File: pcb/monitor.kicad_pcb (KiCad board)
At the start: 2 copper layers, 53 parts, among them K101 CONNECT_2, K102 CONNECT_2, K103 CONNECT_2, K104 CONNECT_2, K105 CONNECT_2, K106 CONNECT_2, K107 CONNECT_2, K108 CONNECT_2, K109 CONNECT_2, K110 CONNECT_2, K111 CONNECT_2, K112 CONNECT_2, T101 ZUMT718, T102 ZUMT718, U101 LTC6803-3

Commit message: Updated files for newer version of kicad
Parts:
- C101, C102, C103, C104, C105, C106, C107, C108, C109, C110, C111, C112: footprint rcl-C0805 -> oshec_rcl:rcl-C0805
- D101, D102, D103, D104, D105, D106, D107, D108, D109, D110, D111, D112: footprint diode-1-SMB -> oshec_diode:diode-1-DO214AA
- K101, K102, K103, K104, K105, K106, K107, K108, K109, K110, K111, K112: footprint CONNECT_2_2mm54_VERT -> Aalto_connect:CONNECT_2_2mm54_VERT
- R101, R102, R103, R104, R105, R106, R107, R108, R109, R110, R111, R112, R113, R114: footprint rcl-R0805 -> oshec_rcl:rcl-C0805
- T101, T102: footprint transistor-SOT23-BEC -> oshec_transistor:transistor-SOT23-BEC
- U101: footprint SSOP44 -> Aalto_ic:SSOP44

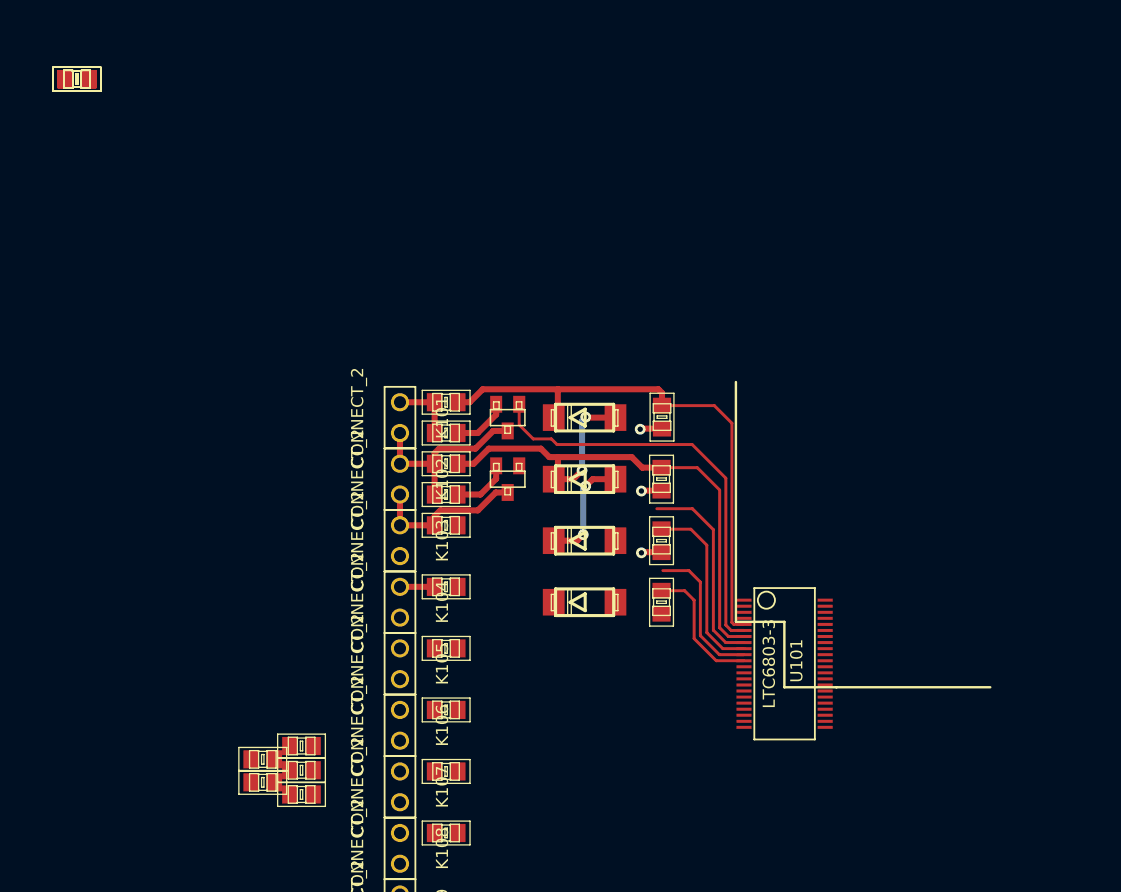
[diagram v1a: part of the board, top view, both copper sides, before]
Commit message: Added few footprints, matched components for footprints
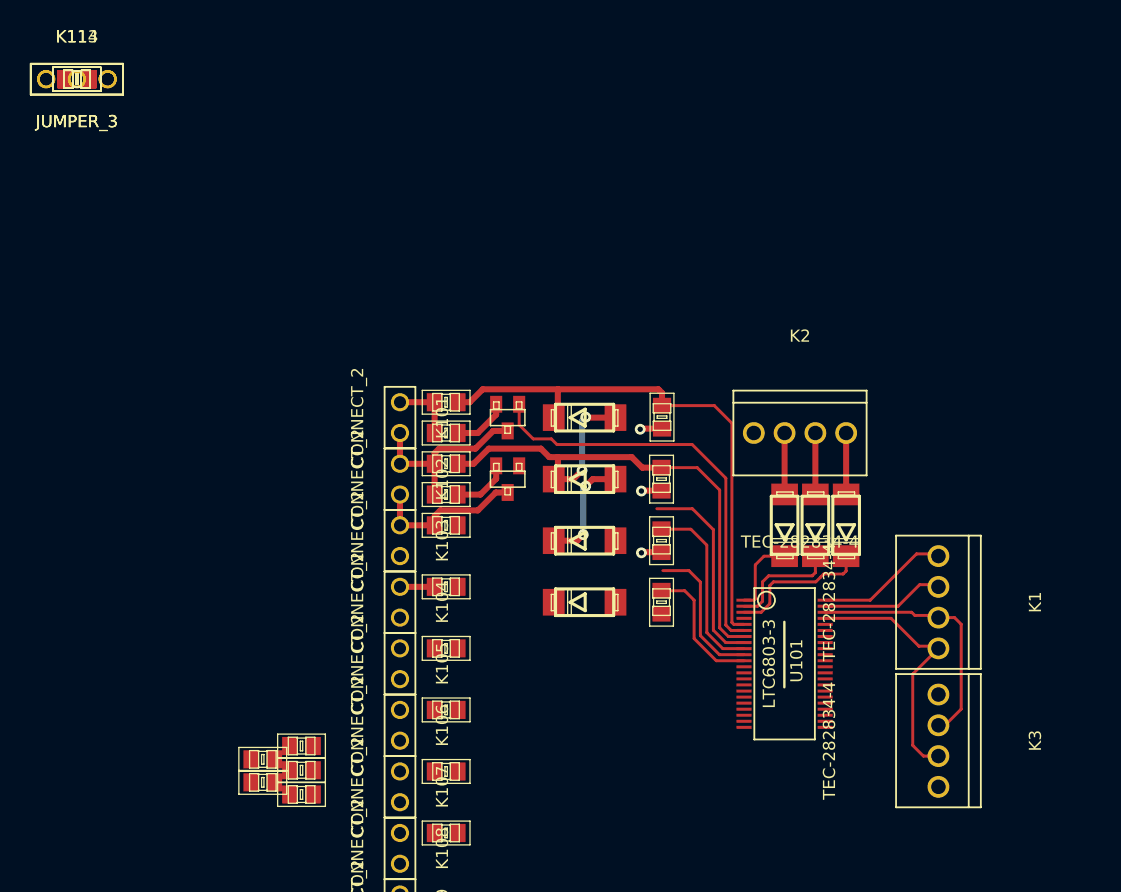
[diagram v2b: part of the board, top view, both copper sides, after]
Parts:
- added D1: ER1J, oshec_diode:diode-1-DO214AA, F.Cu at (58.4, 36.8)
- added D2: ER1J, oshec_diode:diode-1-DO214AA, F.Cu at (61.0, 36.8)
- added D3: ER1J, oshec_diode:diode-1-DO214AA, F.Cu at (63.5, 36.8)
- added K1: TEC-282834-4, Aalto_connect:CONNECT_4_2.54mm_SCREW_TECONNECTIVITY_282834-4, F.Cu at (71.1, 43.2)
- added K113, K114: JUMPER_3, Aalto_connect:JUMPER_3, F.Cu at (0.00, 0.00)
- added K2: TEC-282834-4, Aalto_connect:CONNECT_4_2.54mm_SCREW_TECONNECTIVITY_282834-4, F.Cu at (59.7, 29.2)
- added K3: TEC-282834-4, Aalto_connect:CONNECT_4_2.54mm_SCREW_TECONNECTIVITY_282834-4, F.Cu at (71.1, 54.6)
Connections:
- U101 pad 1: N-0000060 -> /CSBO
- U101 pad 2: N-0000036 -> /SDOI
- U101 pad 3: N-0000035 -> /SCKO
- U101 pad 41: N-0000033 -> /SCKI
- U101 pad 42: N-0000031 -> /SDI
- U101 pad 43: N-0000029 -> /SDO
- U101 pad 44: N-0000045 -> /CSBI
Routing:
- net /SCKI: track 0.00 -> 21.9 mm
- net /SDI: track 0.00 -> 21.2 mm
- net /SCKO: track 0.00 -> 11.9 mm
- net /CSBI: track 0.00 -> 11.1 mm
- net /SDO: track 0.00 -> 10.3 mm
- net /SDOI: track 0.00 -> 9.34 mm
- net /CSBO: track 0.00 -> 6.49 mm
- net Net-(D3-PadA): track 0.00 -> 5.07 mm
- net Net-(D2-PadA): track 0.00 -> 5.07 mm
- net Net-(D1-PadA): track 0.00 -> 5.07 mm

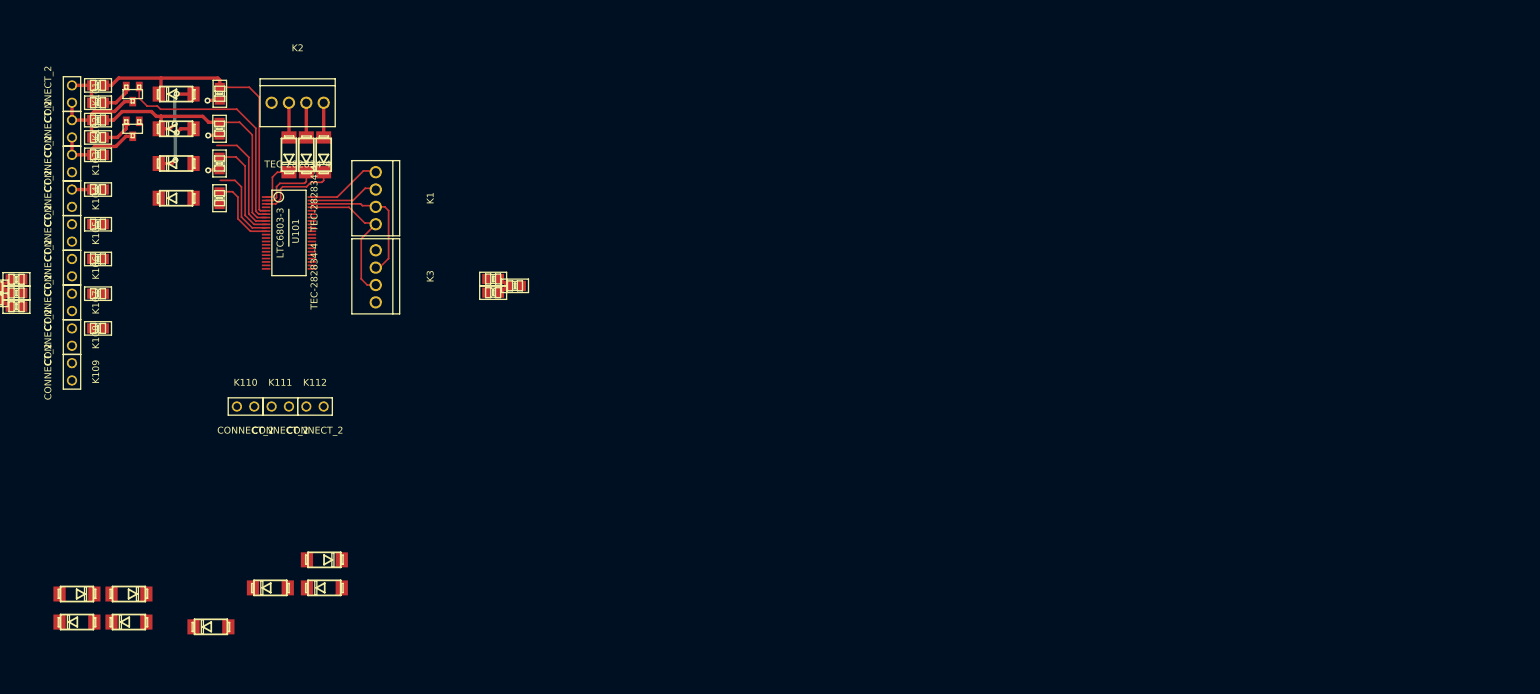
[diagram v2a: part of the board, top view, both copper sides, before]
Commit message: Enlargened board
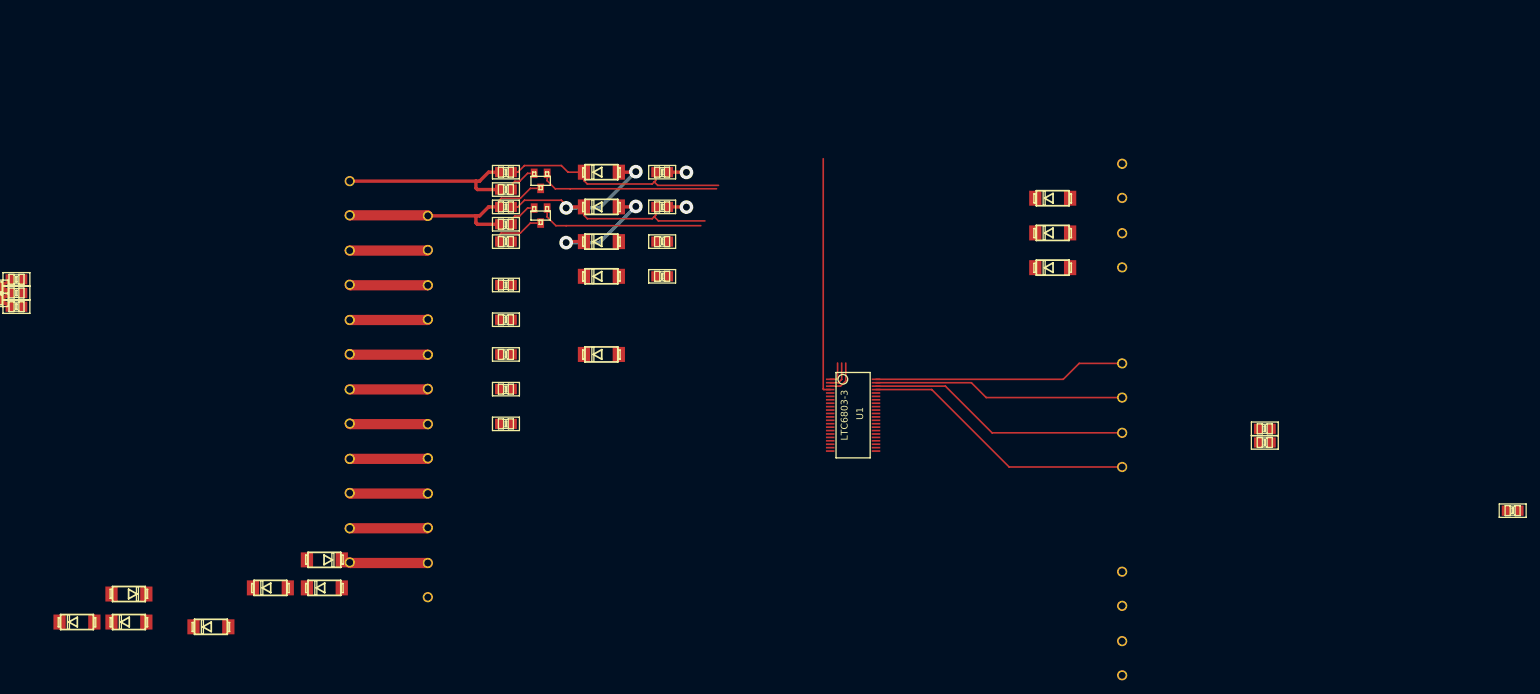
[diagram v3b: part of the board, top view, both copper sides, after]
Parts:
- removed U101: LTC6803-3, Aalto_ic:SSOP44
- added K4: DG128-02P, Aalto_connect:CONNECT_2_5.00mm_SCREW_DG128-02P_DG128-5.0-02P-14-00A(H), B.Cu at (180.3, 50.8)
- added K5: DG128-02P, Aalto_connect:CONNECT_2_5.00mm_SCREW_DG128-02P_DG128-5.0-02P-14-00A(H), B.Cu at (180.3, 100.3)
- added K6: DG128-02P, Aalto_connect:CONNECT_2_5.00mm_SCREW_DG128-02P_DG128-5.0-02P-14-00A(H), B.Cu at (180.3, 110.5)
- added U1: LTC6803-3, Aalto_ic:SSOP44, F.Cu at (141.0, 74.9)
- K1, K2, K3: value TEC-282834-4 -> DG128-02P; footprint Aalto_connect:CONNECT_4_2.54mm_SCREW_TECONNECTIVITY_282834-4 -> Aalto_connect:CONNECT_2_5.00mm_SCREW_DG128-02P_DG128-5.0-02P-14-00A(H); moved to B.Cu
- K101, K102, K103, K104, K105, K106, K107, K108, K109, K110, K111, K112: value CONNECT_2 -> DG128-02P; footprint Aalto_connect:CONNECT_2_2mm54_VERT -> Aalto_connect:CONNECT_2_5.00mm_SCREW_DG128-02P_DG128-5.0-02P-14-00A(H); moved to B.Cu
- K113, K114: footprint Aalto_connect:JUMPER_3 -> Aalto_connect:JUMPER_3_2.54mm
- moved C111 149.7 mm to (237.5, 88.9)
- moved K2 130.9 mm to (180.3, 80.0), turned to 90 degrees
- moved C110 115.0 mm to (201.2, 78.9)
- moved C112 115.0 mm to (201.2, 76.9)
- moved K1 112.4 mm to (180.3, 69.8), turned to 90 degrees
- moved D1 111.9 mm to (170.2, 43.2), turned to 0 degrees
- moved K3 110.1 mm to (180.3, 40.6), turned to 90 degrees
- moved D2 109.8 mm to (170.2, 48.3), turned to 0 degrees
- moved D3 108.0 mm to (170.2, 53.3), turned to 0 degrees
- moved D106 84.4 mm to (104.1, 66.0), turned to 0 degrees
- moved C102 65.8 mm to (113.0, 44.5), turned to 180 degrees
- moved C103 65.8 mm to (113.0, 49.5), turned to 180 degrees
- moved C104 65.8 mm to (113.0, 54.6), turned to 180 degrees
- moved C101 65.7 mm to (113.0, 39.4), turned to 180 degrees
- moved D101 63.3 mm to (104.1, 39.4)
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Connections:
- K2 pad 1: /BATT12+ -> /SDI
- K2 pad 2: Net-(D1-PadA) -> /SCKI
- K3 pad 1: /BATT1- -> /BATT12+
- K3 pad 2: /SDI -> Net-(D1-PadA)
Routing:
- net /V+: track 0.00 -> 34.8 mm
- net /BATT11+: track 15.6 -> 46.2 mm
- net /SDO: track 10.3 -> 36.9 mm
- net /CSBI: track 11.1 -> 37.0 mm
- net /BATT12+: track 5.40 -> 27.0 mm
- net /SCKI: track 21.9 -> 40.7 mm
- net /SDI: track 21.2 -> 38.8 mm
- net /S10: track 12.2 -> 0.00 mm
- net Net-(K109-Pad2): track 0.00 -> 11.5 mm
- net Net-(K111-Pad2): track 0.00 -> 11.5 mm
- net Net-(K110-Pad2): track 0.00 -> 11.5 mm
- net Net-(K108-Pad2): track 0.00 -> 11.5 mm
- net Net-(K107-Pad2): track 0.00 -> 11.5 mm
- net Net-(K106-Pad2): track 0.00 -> 11.5 mm
- net Net-(K105-Pad2): track 0.00 -> 11.5 mm
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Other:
- board text added: "100x100 - factory"
- board text added: "150x100 - factory"
- board text added: "160x100 manual"
- board text added: "50x100 - factory"
- board text added: "80x100 - manual"
- board text added: "ISOLATE ?"
- board text added: "No tracks allowed inside rectangles except ground"
- board text added: "Through-hole components are flipped They're on bottom side of board. This way they get soldered to front"

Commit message: Matched pcb with schematic
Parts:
- added C113: 3u3, oshec_rcl:rcl-C1206, F.Cu at (-40.6, 10.2)
- added LD1: GREEN-LED0805, oshec_led:led-CHIP-LED0805, F.Cu at (92.7, 41.9)
- added LD10: GREEN-LED0805, oshec_led:led-CHIP-LED0805, F.Cu at (-2.54, 40.6)
- added LD11: GREEN-LED0805, oshec_led:led-CHIP-LED0805, F.Cu at (-2.54, 44.5)
- added LD12: GREEN-LED0805, oshec_led:led-CHIP-LED0805, F.Cu at (-2.54, 48.3)
- added LD2: GREEN-LED0805, oshec_led:led-CHIP-LED0805, F.Cu at (92.7, 47.0)
- added LD3: GREEN-LED0805, oshec_led:led-CHIP-LED0805, F.Cu at (92.7, 52.1)
- added LD4: GREEN-LED0805, oshec_led:led-CHIP-LED0805, F.Cu at (92.7, 57.1)
- added LD5: GREEN-LED0805, oshec_led:led-CHIP-LED0805, F.Cu at (-2.54, 21.6)
- added LD6: GREEN-LED0805, oshec_led:led-CHIP-LED0805, F.Cu at (-2.54, 25.4)
- added LD7: GREEN-LED0805, oshec_led:led-CHIP-LED0805, F.Cu at (-2.54, 29.2)
- added LD8: GREEN-LED0805, oshec_led:led-CHIP-LED0805, F.Cu at (-2.54, 33.0)
- added LD9: GREEN-LED0805, oshec_led:led-CHIP-LED0805, F.Cu at (-2.54, 36.8)
- added R1: 10k, oshec_rcl:rcl-R0805, F.Cu at (102.9, 41.9)
- added R10: 100, oshec_rcl:rcl-R0805, F.Cu at (87.6, 57.1)
- added R11: 100, oshec_rcl:rcl-R0805, F.Cu at (-30.5, 5.08)
- added R12: 100, oshec_rcl:rcl-R0805, F.Cu at (-30.5, 8.89)
- added R13: 10k, oshec_rcl:rcl-R0805, F.Cu at (-30.5, 12.7)
- added R14: 10k, oshec_rcl:rcl-R0805, F.Cu at (-30.5, 16.5)
- added R15: 10k, oshec_rcl:rcl-R0805, F.Cu at (-30.5, 20.3)
- added R16: 10k, oshec_rcl:rcl-R0805, F.Cu at (-30.5, 24.1)
- added R17: 10k, oshec_rcl:rcl-R0805, F.Cu at (-30.5, 27.9)
- added R18: 10k, oshec_rcl:rcl-R0805, F.Cu at (-30.5, 31.8)
- added R19: 100, oshec_rcl:rcl-R0805, F.Cu at (-30.5, 35.6)
- added R2: 10k, oshec_rcl:rcl-R0805, F.Cu at (102.9, 47.0)
- added R20: 100, oshec_rcl:rcl-R0805, F.Cu at (-30.5, 39.4)
- added R21: 100, oshec_rcl:rcl-R0805, F.Cu at (-22.9, -33.0)
- added R22: 100, oshec_rcl:rcl-R0805, F.Cu at (-22.9, -29.2)
- added R23: 100, oshec_rcl:rcl-R0805, F.Cu at (-22.9, -25.4)
- added R24: 100, oshec_rcl:rcl-R0805, F.Cu at (-22.9, -21.6)
- added R3: 10k, oshec_rcl:rcl-R0805, F.Cu at (102.9, 52.1)
- added R4: 10k, oshec_rcl:rcl-R0805, F.Cu at (-30.5, -21.6)
- added R5: 10k, oshec_rcl:rcl-R0805, F.Cu at (-30.5, -17.8)
- added R6: 10k, oshec_rcl:rcl-R0805, F.Cu at (-30.5, -14.0)
- added R7: 100, oshec_rcl:rcl-R0805, F.Cu at (87.6, 41.9)
- added R8: 100, oshec_rcl:rcl-R0805, F.Cu at (87.6, 47.0)
- added R9: 100, oshec_rcl:rcl-R0805, F.Cu at (87.6, 52.1)
- added T1: ZUMT718, oshec_transistor:transistor-SOT23-BEC, F.Cu at (97.8, 50.8)
- added T10: ZUMT718, oshec_transistor:transistor-SOT23-BEC, F.Cu at (-61.0, 29.2)
- added T2: ZUMT718, oshec_transistor:transistor-SOT23-BEC, F.Cu at (-68.6, 16.5)
- added T3: ZUMT718, oshec_transistor:transistor-SOT23-BEC, F.Cu at (-68.6, 22.9)
- added T4: ZUMT718, oshec_transistor:transistor-SOT23-BEC, F.Cu at (-68.6, 29.2)
- added T5: ZUMT718, oshec_transistor:transistor-SOT23-BEC, F.Cu at (-68.6, 36.8)
- added T6: ZUMT718, oshec_transistor:transistor-SOT23-BEC, F.Cu at (-68.6, 44.5)
- added T7: ZUMT718, oshec_transistor:transistor-SOT23-BEC, F.Cu at (-61.0, 10.2)
- added T8: ZUMT718, oshec_transistor:transistor-SOT23-BEC, F.Cu at (-61.0, 16.5)
- added T9: ZUMT718, oshec_transistor:transistor-SOT23-BEC, F.Cu at (-61.0, 22.9)
- C101, C102, C103, C104, C105, C106, C107, C108, C109, C110, C111, C112: value 100n -> 3u3; footprint oshec_rcl:rcl-C0805 -> oshec_rcl:rcl-C1206
- R101, R102, R103, R104, R105, R106, R107, R108, R109, R110, R111, R112: value 100R -> 10k
- R113: value R-EU_R0805 -> 10k
- moved R112 84.2 mm to (-16.5, 82.5)
- moved R111 80.5 mm to (-16.5, 78.7)
- moved R110 76.7 mm to (-16.5, 74.9)
- moved R109 73.0 mm to (-16.5, 71.1)
- moved R113 59.7 mm to (88.9, 101.6)
- moved R105 28.7 mm to (96.5, 88.9)
- moved R114 28.7 mm to (96.5, 74.9)
- moved D104 28.7 mm to (110.5, 82.5)
- moved D106 28.7 mm to (110.5, 94.0)
- moved R106 28.7 mm to (96.5, 94.0)
- moved R107 28.7 mm to (96.5, 99.1)
- moved R108 28.7 mm to (96.5, 104.1)
- moved R104 28.7 mm to (96.5, 83.8)
- moved C103 26.4 mm to (128.3, 71.1)
- moved C104 26.4 mm to (128.3, 76.2)
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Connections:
- net Net-(K103-Pad2) renamed /BATT9+
- net Net-(K104-Pad2) renamed /BATT8+
- net Net-(K105-Pad2) renamed /BATT7+
- net Net-(K106-Pad2) renamed /BATT6+
- net Net-(K107-Pad2) renamed /BATT5+
- net Net-(K108-Pad2) renamed /BATT4+
- net Net-(K109-Pad2) renamed /BATT3+
- net Net-(K110-Pad2) renamed /BATT2+
- net Net-(K111-Pad2) renamed /BATT1+
- D112 pad A: GND -> Net-(C113-Pad2)
- R113 pad 1: Net-(R113-Pad1) -> Net-(C113-Pad2)
- R113 pad 2: /BATT12+ -> GND
- T101 pad B: /S12 -> Net-(R1-Pad2)
- T101 pad C: /BATT11+ -> Net-(LD1-PadA)
- T101 pad E: Net-(R113-Pad1) -> /BATT12+
- T102 pad B: /S11 -> Net-(R2-Pad2)
- T102 pad C: /BATT10+ -> Net-(LD2-PadA)
- T102 pad E: Net-(R114-Pad1) -> /BATT11+
- U1 pad 29: GND -> Net-(C113-Pad2)
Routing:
- net Net-(C102-Pad2): track 49.9 -> 0.00 mm, vias 2 -> 0
- net /BATT11+: track 46.2 -> 11.5 mm
- net Net-(C101-Pad2): track 34.3 -> 0.00 mm
- net /S12: track 26.3 -> 0.00 mm
- net /S11: track 24.3 -> 0.00 mm
- net Net-(C103-Pad2): track 17.6 -> 0.00 mm, vias 2 -> 0
- net /BATT12+: track 27.0 -> 37.1 mm
- net /BATT10+: track 19.2 -> 11.5 mm
- net Net-(R114-Pad1): track 4.66 -> 0.00 mm
- net Net-(R113-Pad1): track 4.66 -> 0.00 mm
- net Net-(LD1-PadA): track 0.00 -> 3.91 mm
- net Net-(R1-Pad2): track 0.00 -> 3.16 mm
- net Net-(LD1-PadC): track 0.00 -> 3.08 mm
- net GND: track 5.22 -> 2.61 mm, vias 2 -> 1
